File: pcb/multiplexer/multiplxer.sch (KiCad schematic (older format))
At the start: 8 parts, among them J1 Conn_01x04, U1 74HC595, U2 4051

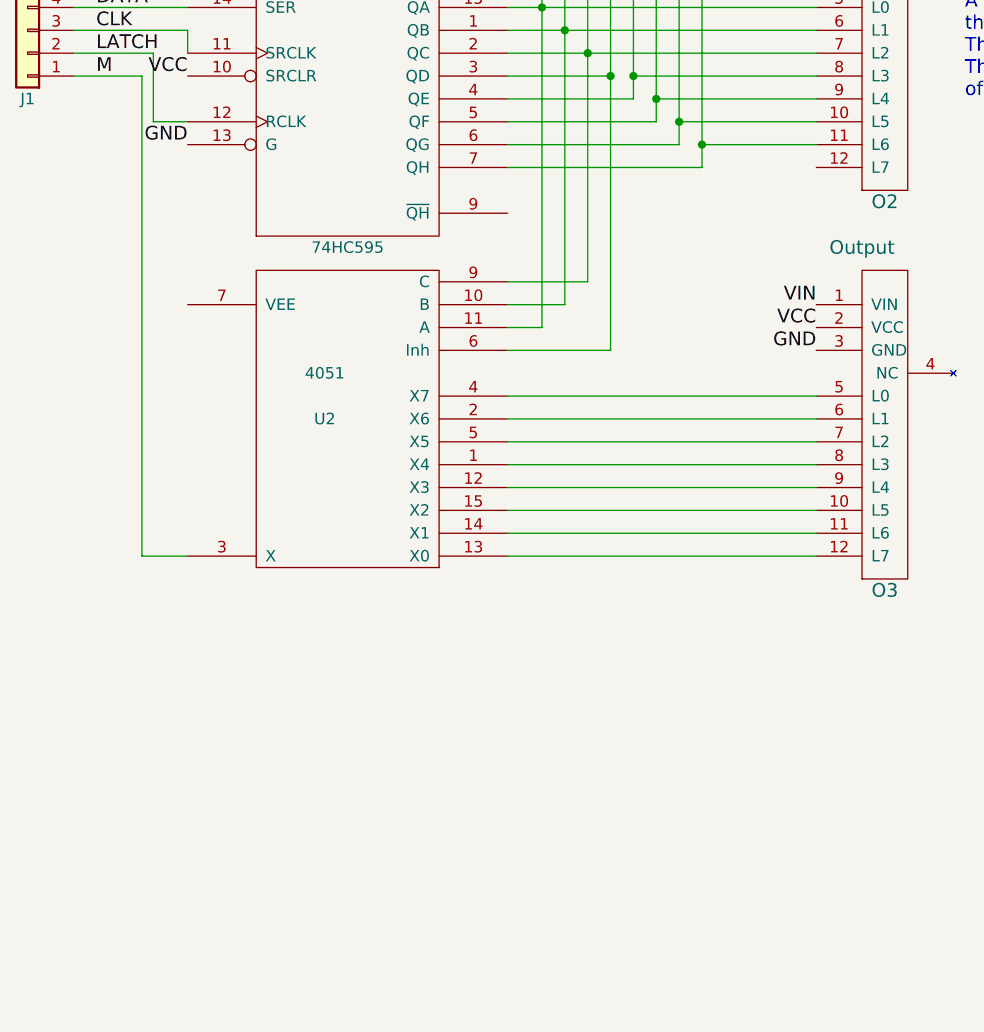
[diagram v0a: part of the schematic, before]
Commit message: Added README.md for each of the modules, plus a few minor tweaks to PCB layouts while writing the text.
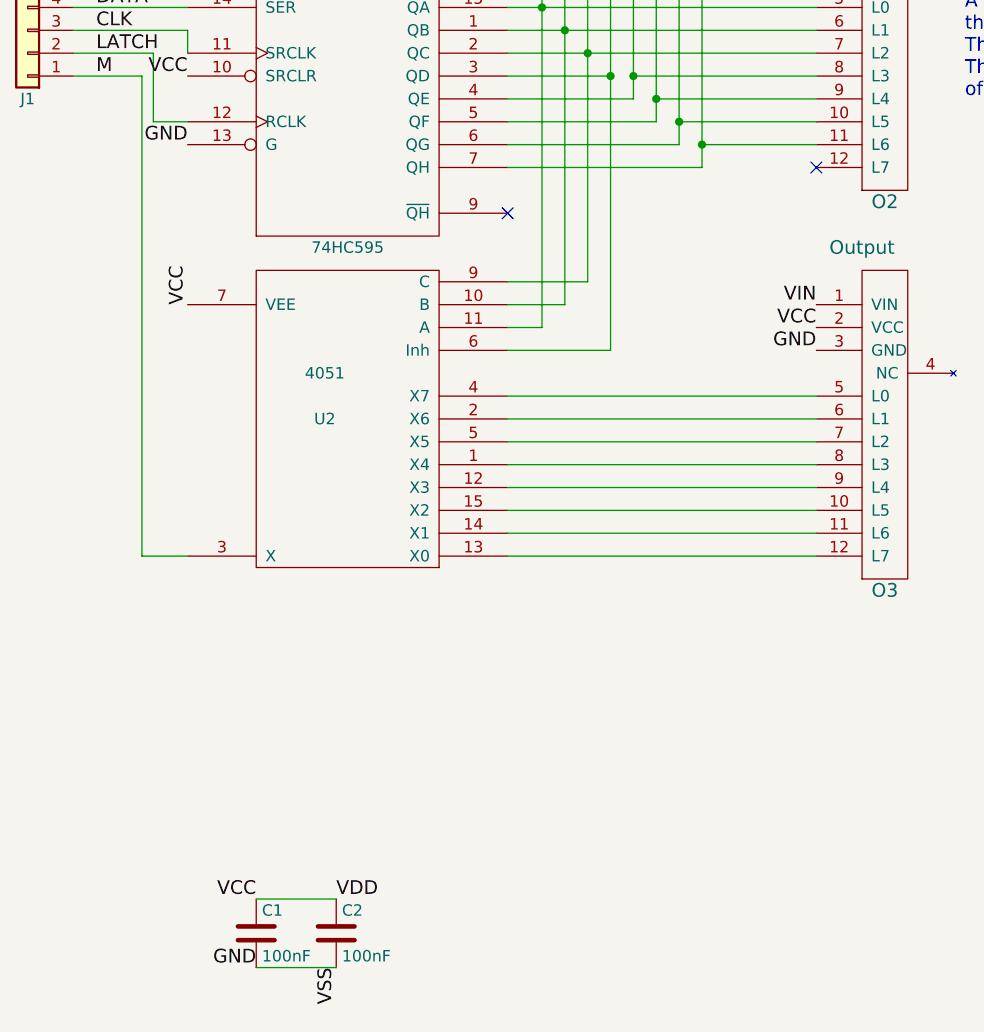
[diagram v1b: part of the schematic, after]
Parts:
- added C1, C2: 100nF, Capacitors_THT:C_Disc_D3.8mm_W2.6mm_P2.50mm, symbol C
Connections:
- net VDD is gone; now on net VCC: U2.16 (VDD)
- net VSS is gone; now on net Earth: U2.8 (VSS)
- net Earth: now also C1.2, C2.2
- net VCC: now also U2.7 (VEE), C1.1, C2.1
- no-connect marks 0 -> 2
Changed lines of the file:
@@
 Text Label 4000 2850 0    60   ~ 0
 M
+$Comp
+L C C2
+U 1 1 5AF991BA
+P 5050 6600
+F 0 "C2" H 5075 6700 50  0000 L CNN
+F 1 "100nF" H 5075 6500 50  0000 L CNN
+F 2 "Capacitors_THT:C_Disc_D3.8mm_W2.6mm_P2.50mm" H 5088 6450 50  0001 C CNN
+F 3 "" H 5050 6600 50  0001 C CNN
+	1    5050 6600
+	1    0    0    -1
+$EndComp
+$Comp
+L C C1
+U 1 1 5AF99270
+P 4700 6600
+F 0 "C1" H 4725 6700 50  0000 L CNN
+F 1 "100nF" H 4725 6500 50  0000 L CNN
+F 2 "Capacitors_THT:C_Disc_D3.8mm_W2.6mm_P2.50mm" H 4738 6450 50  0001 C CNN
+F 3 "" H 4700 6600 50  0001 C CNN
+	1    4700 6600
+	1    0    0    -1
+$EndComp
+Wire Wire Line
+	4700 6450 5050 6450
+Wire Wire Line
+	4700 6750 5050 6750
+Text Label 4700 6750 2    60   ~ 0
+GND
+Text Label 4700 6450 2    60   ~ 0
+VCC
+Text Label 4400 3850 1    60   ~ 0
+VCC
+Text Label 5050 6450 0    60   ~ 0
+VDD
+Text Label 5050 6750 3    60   ~ 0
+VSS
+NoConn ~ 5800 3450
+NoConn ~ 7150 3250
 $EndSCHEMATC
